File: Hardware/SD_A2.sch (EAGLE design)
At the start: 32 parts, among them IC1 74LS245N, IC2 LM317, IC3 2716 / 2732, IC4 XC9572XL

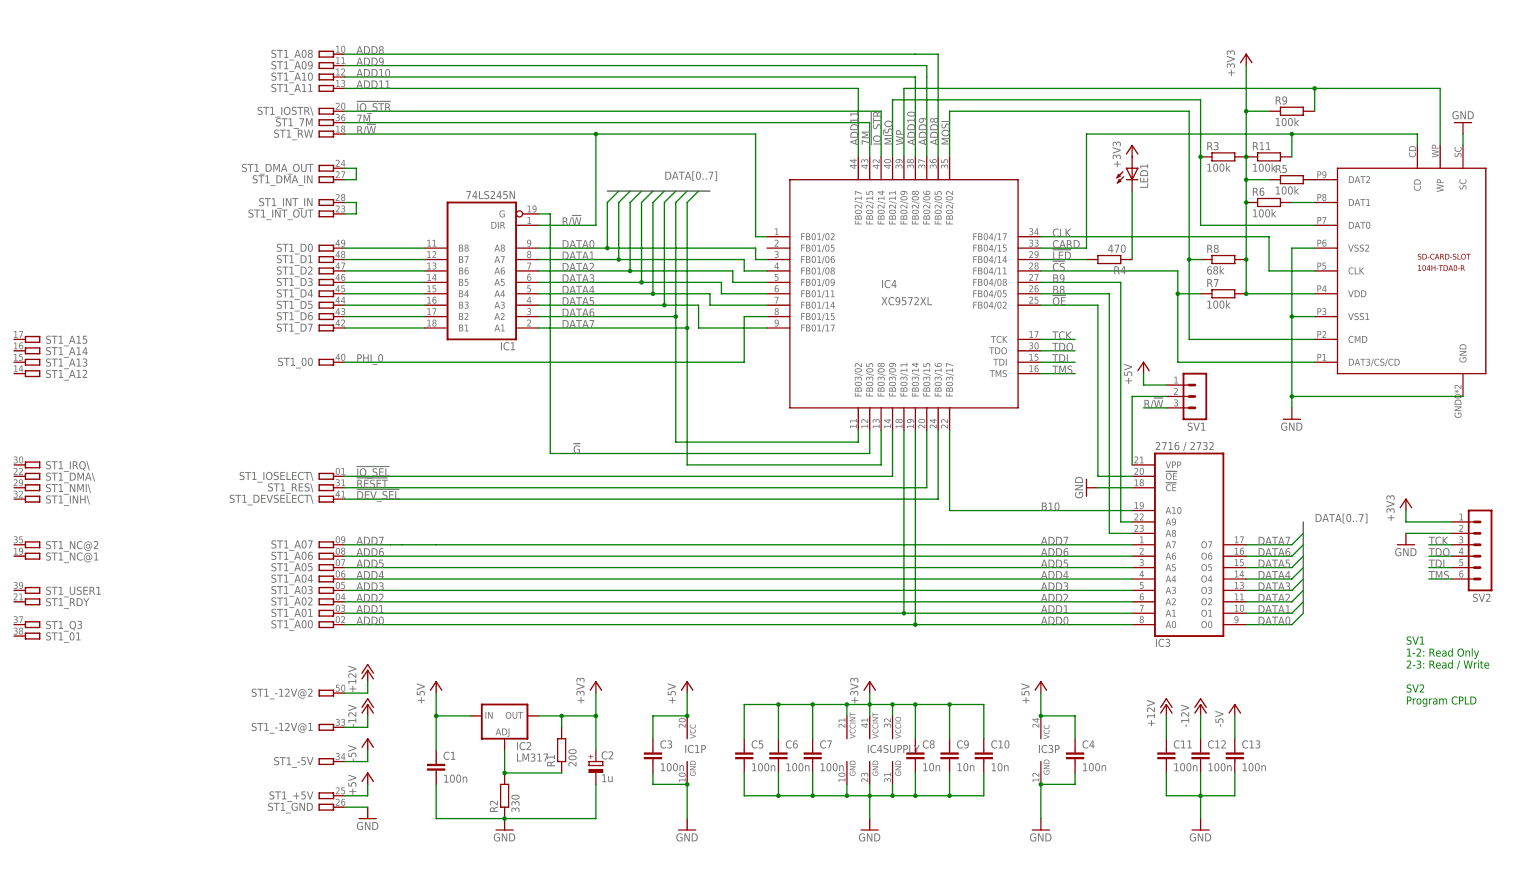
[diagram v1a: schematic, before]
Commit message: NWE added to schematic and layout
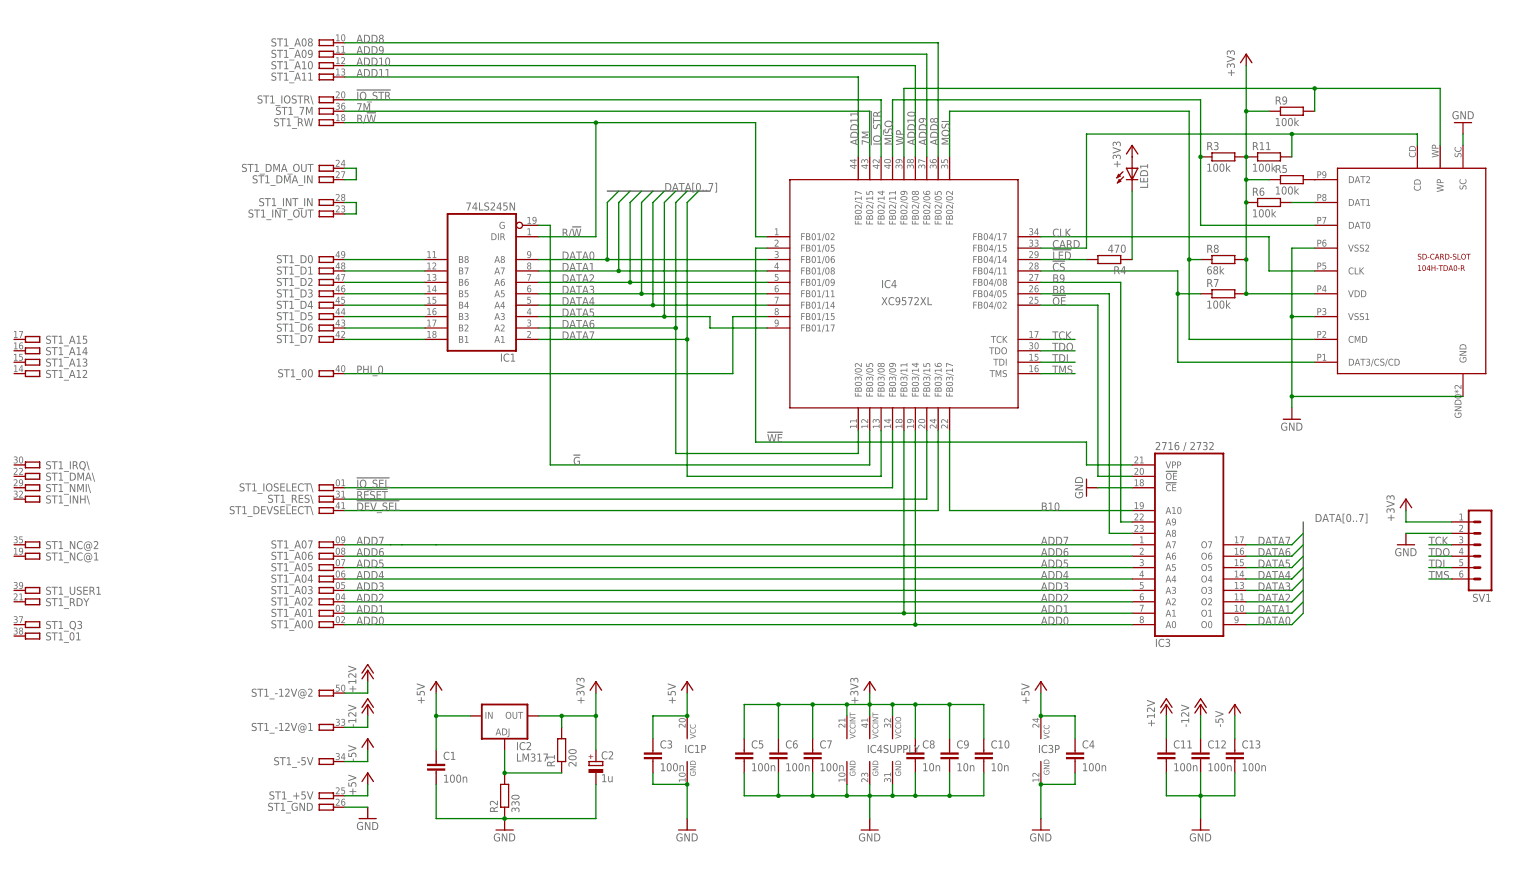
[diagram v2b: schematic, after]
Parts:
- removed SV2: (no value), con-lstb:MA06-1
- SV1: device con-lstb:MA03-1 -> con-lstb:MA06-1
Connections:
- removed net VPP: IC3A.VPP, SV1.2
- new net !WE: IC3A.VPP, IC4G$1.FB01/05
- net +3V3: now also SV1.1; no longer SV2.1
- net +5V: no longer SV1.1
- net GND: now also SV1.2; no longer SV2.2
- net R/!W: no longer SV1.3
- net TCK: now also SV1.3; no longer SV2.3
- net TDI: now also SV1.5; no longer SV2.5
- net TDO: now also SV1.4; no longer SV2.4
- net TMS: now also SV1.6; no longer SV2.6
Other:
- note removed: "SV1 1-2: Read Only 2-3: Read / Write SV2 Program CPLD"
- moved on the sheet: IC1, ST1_00, ST1_7M, ST1_A08, ST1_A09, ST1_A10, ST1_A11, ST1_D0, ST1_D1, ST1_D2, ST1_D3, ST1_D4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

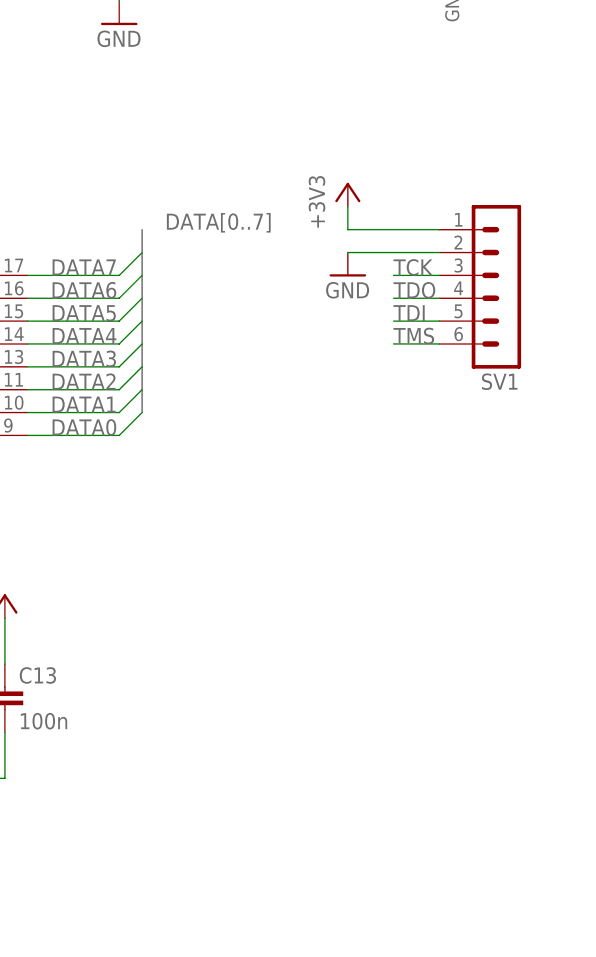
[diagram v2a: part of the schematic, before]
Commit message: Tag Connect added
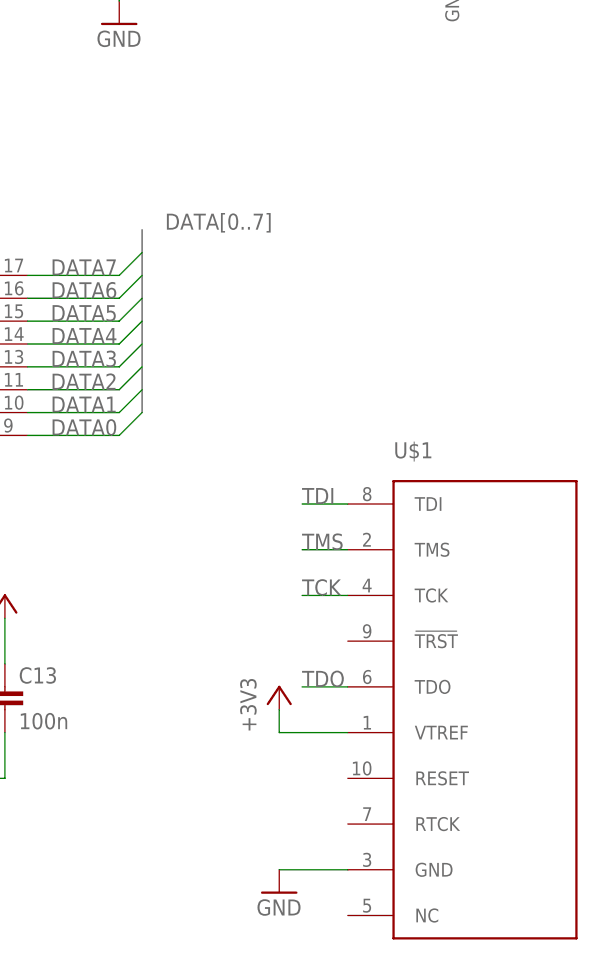
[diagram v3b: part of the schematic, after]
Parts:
- removed SV1: (no value), con-lstb:MA06-1
- added U$1: TC2050-NL, eagle_tag-connect-2050:TC2050-NL
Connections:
- net +3V3: now also U$1.VTREF; no longer SV1.1
- net GND: now also U$1.GND; no longer SV1.2
- net TCK: now also U$1.TCK; no longer SV1.3
- net TDI: now also U$1.TDI; no longer SV1.5
- net TDO: now also U$1.TDO; no longer SV1.4
- net TMS: now also U$1.TMS; no longer SV1.6
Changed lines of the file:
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@@
 <layer number="51" name="tDocu" color="7" fill="1" visible="no" active="no"/>
 <layer number="52" name="bDocu" color="7" fill="1" visible="no" active="no"/>
+<layer number="53" name="tGND_GNDA" color="7" fill="9" visible="no" active="no"/>
+<layer number="54" name="bGND_GNDA" color="1" fill="9" visible="no" active="no"/>
 <layer number="56" name="wert" color="7" fill="1" visible="no" active="no"/>
 <layer number="90" name="Modules" color="5" fill="1" visible="yes" active="yes"/>
@@
 <layer number="97" name="Info" color="7" fill="1" visible="yes" active="yes"/>
 <layer number="98" name="Guide" color="6" fill="1" visible="yes" active="yes"/>
+<layer number="100" name="Release" color="7" fill="1" visible="no" active="yes"/>
+<layer number="101" name="Heatsink" color="7" fill="1" visible="no" active="yes"/>
+<layer number="102" name="tMarkings" color="7" fill="1" visible="no" active="yes"/>
+<layer number="103" name="bMarkings" color="7" fill="1" visible="no" active="yes"/>
+<layer number="104" name="Name" color="7" fill="1" visible="no" active="yes"/>
 <layer number="105" name="Beschreib" color="7" fill="1" visible="yes" active="yes"/>
 <layer number="106" name="BGA-Top" color="7" fill="1" visible="yes" active="yes"/>
 <layer number="107" name="BD-Top" color="7" fill="1" visible="yes" active="yes"/>
+<layer number="116" name="Patch_BOT" color="9" fill="4" visible="no" active="yes"/>
+<layer number="121" name="_layer121" color="7" fill="1" visible="no" active="yes"/>
+<layer number="122" name="_bplace" color="7" fill="1" visible="no" active="yes"/>
+<layer number="150" name="References" color="7" fill="1" visible="no" active="yes"/>
+<layer number="151" name="HeatSink" color="14" fill="1" visible="no" active="no"/>
 <layer number="200" name="200bmp" color="7" fill="1" visible="yes" active="yes"/>
+<layer number="201" name="201bmp" color="2" fill="10" visible="no" active="yes"/>
+<layer number="202" name="202bmp" color="3" fill="10" visible="no" active="yes"/>
+<layer number="203" name="203bmp" color="4" fill="10" visible="no" active="yes"/>
+<layer number="204" name="204bmp" color="5" fill="10" visible="no" active="yes"/>
+<layer number="205" name="205bmp" color="6" fill="10" visible="no" active="yes"/>
+<layer number="206" name="206bmp" color="7" fill="10" visible="no" active="yes"/>
+<layer number="207" name="207bmp" color="8" fill="10" visible="no" active="yes"/>
+<layer number="208" name="208bmp" color="9" fill="10" visible="no" active="yes"/>
+<layer number="231" name="Eagle3D_PG1" color="14" fill="1" visible="no" active="yes"/>
+<layer number="232" name="Eagle3D_PG2" color="14" fill="2" visible="no" active="yes"/>
+<layer number="233" name="Eagle3D_PG3" color="14" fill="4" visible="no" active="yes"/>
 <layer number="250" name="Descript" color="7" fill="1" visible="yes" active="yes"/>
 <layer number="251" name="SMDround" color="7" fill="1" visible="yes" active="yes"/>
+<layer number="254" name="OrgLBR" color="13" fill="1" visible="no" active="no"/>
 </layers>
 <schematic xreflabel="%F%N/%S.%C%R" xrefpart="/%S.%C%R">
@@
 <part name="R9" library="rcl" deviceset="R-EU_" device="R0603" value="100k"/>
 <part name="GND4" library="supply1" deviceset="GND" device=""/>
-<part name="SV1" library="con-lstb" deviceset="MA06-1" device=""/>
-<part name="+3V3" library="supply1" deviceset="+3V3" device=""/>
-<part name="GND8" library="supply1" deviceset="GND" device=""/>
 <part name="C5" library="rcl" deviceset="C-EU" device="C0603K" value="100n"/>
 <part name="C6" library="rcl" deviceset="C-EU" device="C0603K" value="100n"/>
@@
 <part name="C12" library="rcl" deviceset="C-EU" device="C0603K" value="100n"/>
 <part name="C13" library="rcl" deviceset="C-EU" device="C0603K" value="100n"/>
+<part name="U$1" library="eagle_tag-connect-2050" deviceset="TC2050-NL" device=""/>
+<part name="+3V6" library="supply1" deviceset="+3V3" device=""/>
+<part name="GND11" library="supply1" deviceset="GND" device=""/>
 </parts>
 <sheets>
@@
 <instance part="R9" gate="G$1" x="287.02" y="165.1"/>
 <instance part="GND4" gate="1" x="241.3" y="81.28" rot="R270"/>
-<instance part="SV1" gate="1" x="330.2" y="66.04" rot="R180"/>
-<instance part="+3V3" gate="G$1" x="312.42" y="78.74"/>
-<instance part="GND8" gate="1" x="312.42" y="68.58"/>
 <instance part="C5" gate="G$1" x="165.1" y="22.86"/>
 <instance part="C6" gate="G$1" x="172.72" y="22.86"/>
@@
 <instance part="C12" gate="G$1" x="266.7" y="22.86"/>
 <instance part="C13" gate="G$1" x="274.32" y="22.86"/>
+<instance part="U$1" gate="G$1" x="330.2" y="30.48"/>
+<instance part="+3V6" gate="G$1" x="304.8" y="22.86"/>
+<instance part="GND11" gate="1" x="304.8" y="0"/>
 </instances>
 <busses>
@@
 </segment>
 <segment>
-<pinref part="SV1" gate="1" pin="2"/>
-<wire x1="322.58" y1="71.12" x2="312.42" y2="71.12" width="0.1524" layer="91"/>
-<pinref part="GND8" gate="1" pin="GND"/>
-</segment>
-<segment>
 <pinref part="GND9" gate="1" pin="GND"/>
 <pinref part="U$2" gate="G$1" pin="SC"/>
@@
 <wire x1="274.32" y1="17.78" x2="274.32" y2="12.7" width="0.1524" layer="91"/>
 <wire x1="274.32" y1="12.7" x2="266.7" y2="12.7" width="0.1524" layer="91"/>
+</segment>
+<segment>
+<pinref part="U$1" gate="G$1" pin="GND"/>
+<wire x1="312.42" y1="2.54" x2="304.8" y2="2.54" width="0.1524" layer="91"/>
+<pinref part="GND11" gate="1" pin="GND"/>
 </segment>
 </net>
@@
 </segment>
 <segment>
-<pinref part="SV1" gate="1" pin="1"/>
-<wire x1="322.58" y1="73.66" x2="312.42" y2="73.66" width="0.1524" layer="91"/>
-<wire x1="312.42" y1="73.66" x2="312.42" y2="76.2" width="0.1524" layer="91"/>
-<pinref part="+3V3" gate="G$1" pin="+3V3"/>
+<pinref part="U$1" gate="G$1" pin="VTREF"/>
+<wire x1="312.42" y1="17.78" x2="304.8" y2="17.78" width="0.1524" layer="91"/>
+<wire x1="304.8" y1="17.78" x2="304.8" y2="20.32" width="0.1524" layer="91"/>
+<pinref part="+3V6" gate="G$1" pin="+3V3"/>
 </segment>
 </net>
@@
 </segment>
 <segment>
-<pinref part="SV1" gate="1" pin="3"/>
-<wire x1="322.58" y1="68.58" x2="317.5" y2="68.58" width="0.1524" layer="91"/>
-<label x="317.5" y="68.58" size="1.778" layer="95"/>
+<pinref part="U$1" gate="G$1" pin="TCK"/>
+<wire x1="312.42" y1="33.02" x2="307.34" y2="33.02" width="0.1524" layer="91"/>
+<label x="307.34" y="33.02" size="1.778" layer="95"/>
 </segment>
 </net>
@@
 </segment>
 <segment>
-<pinref part="SV1" gate="1" pin="4"/>
-<wire x1="322.58" y1="66.04" x2="317.5" y2="66.04" width="0.1524" layer="91"/>
-<label x="317.5" y="66.04" size="1.778" layer="95"/>
+<pinref part="U$1" gate="G$1" pin="TDO"/>
+<wire x1="312.42" y1="22.86" x2="307.34" y2="22.86" width="0.1524" layer="91"/>
+<label x="307.34" y="22.86" size="1.778" layer="95"/>
 </segment>
 </net>
@@
 </segment>
 <segment>
-<pinref part="SV1" gate="1" pin="5"/>
-<wire x1="322.58" y1="63.5" x2="317.5" y2="63.5" width="0.1524" layer="91"/>
-<label x="317.5" y="63.5" size="1.778" layer="95"/>
+<pinref part="U$1" gate="G$1" pin="TDI"/>
+<wire x1="312.42" y1="43.18" x2="307.34" y2="43.18" width="0.1524" layer="91"/>
+<label x="307.34" y="43.18" size="1.778" layer="95"/>
 </segment>
 </net>
@@
 </segment>
 <segment>
-<pinref part="SV1" gate="1" pin="6"/>
-<wire x1="322.58" y1="60.96" x2="317.5" y2="60.96" width="0.1524" layer="91"/>
-<label x="317.5" y="60.96" size="1.778" layer="95"/>
-</segment>
-</net>
+<pinref part="U$1" gate="G$1" pin="TMS"/>
+<wire x1="312.42" y1="38.1" x2="307.34" y2="38.1" width="0.1524" layer="91"/>
+<label x="307.34" y="38.1" size="1.778" layer="95"/>
+</segment>
+</net>
